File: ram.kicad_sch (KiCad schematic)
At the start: 8 parts, among them J1 ramslot1, J2 ramslot2, J3 ramslot3, J4 ramslot4, U24 74HC08, U29 74HC32, U30 74HC139

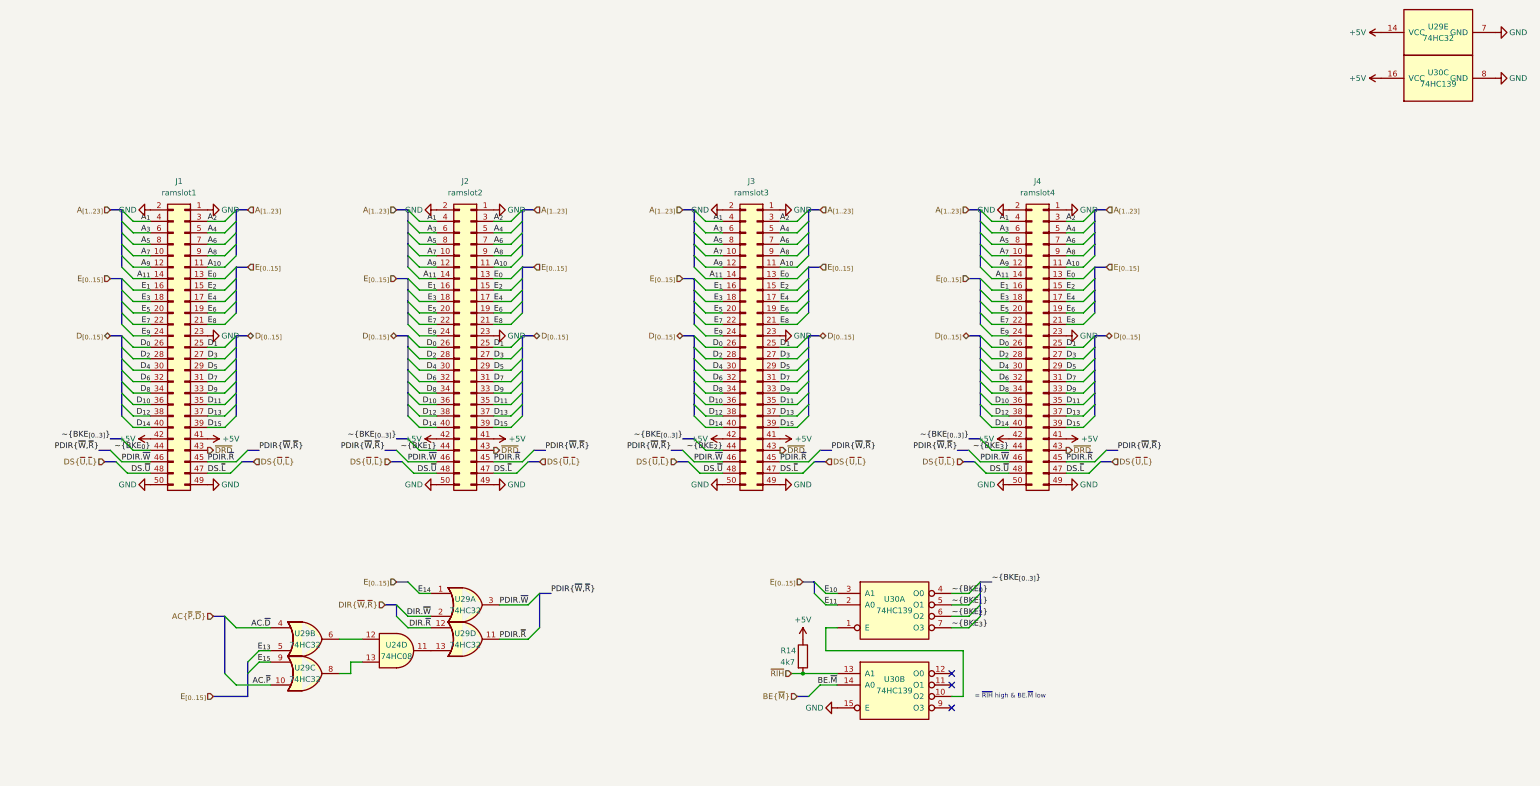
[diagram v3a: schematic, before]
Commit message: first commit: scheme ok [decoder]: 	- new spv. address space [mmu]: 	- removed pidreg 	- switched back to 8Kb mmu rams [ram/peripherals]: 	- added ground pins to connectors [misc]: 	- added DMA support 	- added clock halfer
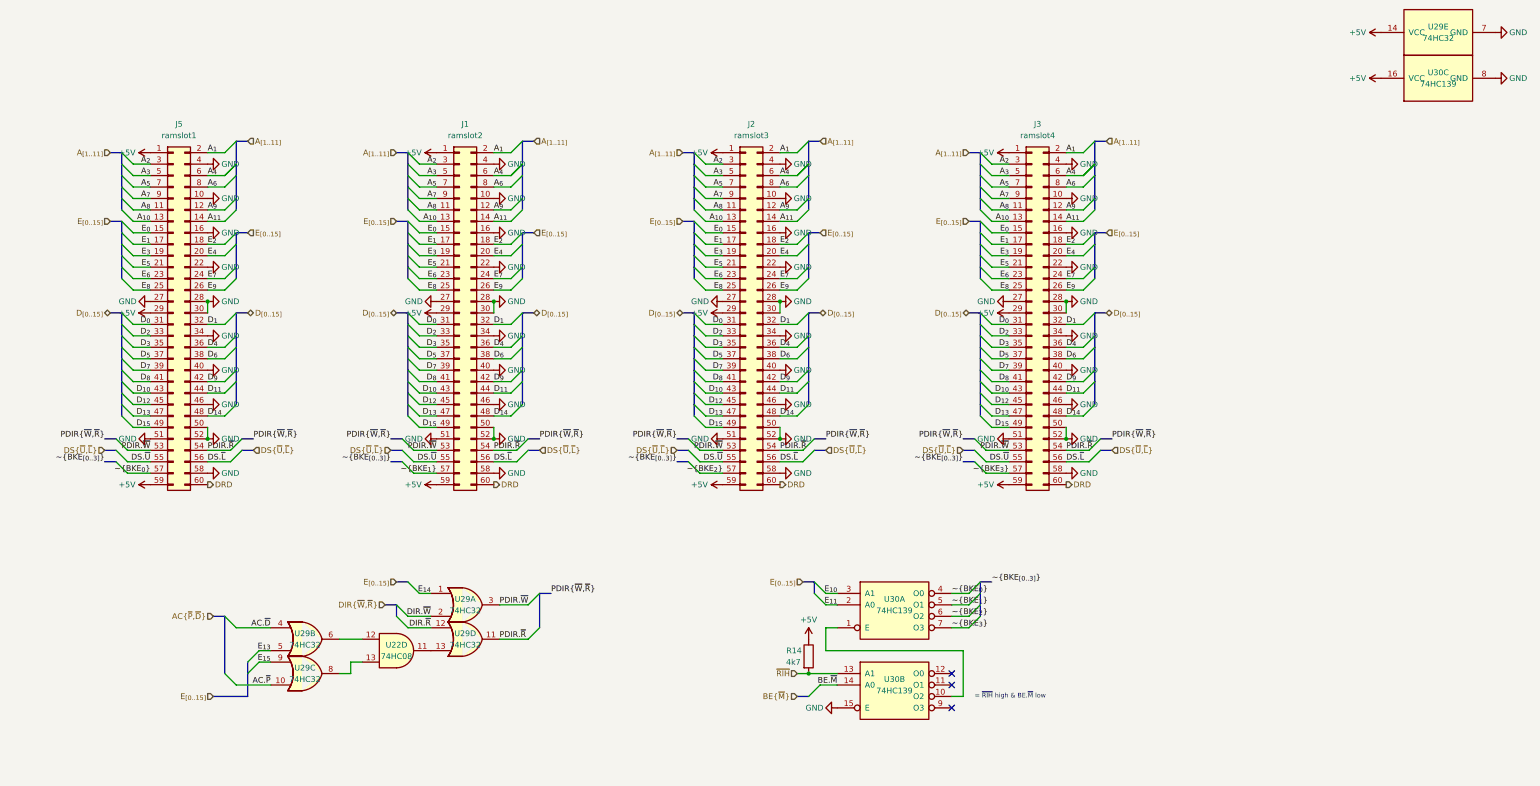
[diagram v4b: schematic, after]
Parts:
- removed J1: ramslot1, Connector_PCBEdge:TE_1-5530843-6, symbol Connector_Generic:Conn_02x25_Odd_Even
- removed J2: ramslot2, Connector_PCBEdge:TE_1-5530843-6, symbol Connector_Generic:Conn_02x25_Odd_Even
- removed J3: ramslot3, Connector_PCBEdge:TE_1-5530843-6, symbol Connector_Generic:Conn_02x25_Odd_Even
- removed J4: ramslot4, Connector_PCBEdge:TE_1-5530843-6, symbol Connector_Generic:Conn_02x25_Odd_Even
- removed U24: 74HC08, Package_DIP:DIP-14_W7.62mm, symbol 74xx:74LS08
- added J1: ramslot2, symbol Connector_Generic:Conn_02x30_Odd_Even
- added J2: ramslot3, symbol Connector_Generic:Conn_02x30_Odd_Even
- added J3: ramslot4, symbol Connector_Generic:Conn_02x30_Odd_Even
- added J5: ramslot1, symbol Connector_Generic:Conn_02x30_Odd_Even
- added U22: 74HC08, symbol 74xx:74LS08
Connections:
- net +5V: now also J1.1 (Pin_1), J1.29 (Pin_29), J1.59 (Pin_59), J2.1 (Pin_1), J2.29 (Pin_29), J2.59 (Pin_59), J3.1 (Pin_1), J3.29 (Pin_29), J3.59 (Pin_59), J5.1 (Pin_1), J5.29 (Pin_29), J5.59 (Pin_59)
- net A_{10}: now also J1.13 (Pin_13), J2.13 (Pin_13), J3.13 (Pin_13), J5.13 (Pin_13)
- net A_{11}: now also J1.14 (Pin_14), J2.14 (Pin_14), J3.14 (Pin_14), J5.14 (Pin_14)
- net A_{1}: now also J1.2 (Pin_2), J2.2 (Pin_2), J3.2 (Pin_2), J5.2 (Pin_2)
- net A_{2}: now also J1.3 (Pin_3), J2.3 (Pin_3), J3.3 (Pin_3), J5.3 (Pin_3)
- net A_{3}: now also J1.5 (Pin_5), J2.5 (Pin_5), J3.5 (Pin_5), J5.5 (Pin_5)
- net A_{4}: now also J1.6 (Pin_6), J2.6 (Pin_6), J3.6 (Pin_6), J5.6 (Pin_6)
- net A_{5}: now also J1.7 (Pin_7), J2.7 (Pin_7), J3.7 (Pin_7), J5.7 (Pin_7)
- net A_{6}: now also J1.8 (Pin_8), J2.8 (Pin_8), J3.8 (Pin_8), J5.8 (Pin_8)
- net A_{7}: now also J1.9 (Pin_9), J2.9 (Pin_9), J3.9 (Pin_9), J5.9 (Pin_9)
- net A_{8}: now also J1.11 (Pin_11), J2.11 (Pin_11), J3.11 (Pin_11), J5.11 (Pin_11)
- net A_{9}: now also J1.12 (Pin_12), J2.12 (Pin_12), J3.12 (Pin_12), J5.12 (Pin_12)
- net DS.~{L}: now also J1.56 (Pin_56), J2.56 (Pin_56), J3.56 (Pin_56), J5.56 (Pin_56)
- net DS.~{U}: now also J1.55 (Pin_55), J2.55 (Pin_55), J3.55 (Pin_55), J5.55 (Pin_55)
- net D_{0}: now also J1.31 (Pin_31), J2.31 (Pin_31), J3.31 (Pin_31), J5.31 (Pin_31)
- net D_{10}: now also J1.43 (Pin_43), J2.43 (Pin_43), J3.43 (Pin_43), J5.43 (Pin_43)
- net D_{11}: now also J1.44 (Pin_44), J2.44 (Pin_44), J3.44 (Pin_44), J5.44 (Pin_44)
- net D_{12}: now also J1.45 (Pin_45), J2.45 (Pin_45), J3.45 (Pin_45), J5.45 (Pin_45)
- net D_{13}: now also J1.47 (Pin_47), J2.47 (Pin_47), J3.47 (Pin_47), J5.47 (Pin_47)
- net D_{14}: now also J1.48 (Pin_48), J2.48 (Pin_48), J3.48 (Pin_48), J5.48 (Pin_48)
- net D_{15}: now also J1.49 (Pin_49), J2.49 (Pin_49), J3.49 (Pin_49), J5.49 (Pin_49)
- net D_{1}: now also J1.32 (Pin_32), J2.32 (Pin_32), J3.32 (Pin_32), J5.32 (Pin_32)
- net D_{2}: now also J1.33 (Pin_33), J2.33 (Pin_33), J3.33 (Pin_33), J5.33 (Pin_33)
- net D_{3}: now also J1.35 (Pin_35), J2.35 (Pin_35), J3.35 (Pin_35), J5.35 (Pin_35)
- net D_{4}: now also J1.36 (Pin_36), J2.36 (Pin_36), J3.36 (Pin_36), J5.36 (Pin_36)
- net D_{5}: now also J1.37 (Pin_37), J2.37 (Pin_37), J3.37 (Pin_37), J5.37 (Pin_37)
- net D_{6}: now also J1.38 (Pin_38), J2.38 (Pin_38), J3.38 (Pin_38), J5.38 (Pin_38)
- net D_{7}: now also J1.39 (Pin_39), J2.39 (Pin_39), J3.39 (Pin_39), J5.39 (Pin_39)
- net D_{8}: now also J1.41 (Pin_41), J2.41 (Pin_41), J3.41 (Pin_41), J5.41 (Pin_41)
- net D_{9}: now also J1.42 (Pin_42), J2.42 (Pin_42), J3.42 (Pin_42), J5.42 (Pin_42)
- net E_{0}: now also J1.15 (Pin_15), J2.15 (Pin_15), J3.15 (Pin_15), J5.15 (Pin_15)
- net E_{1}: now also J1.17 (Pin_17), J2.17 (Pin_17), J3.17 (Pin_17), J5.17 (Pin_17)
- net E_{2}: now also J1.18 (Pin_18), J2.18 (Pin_18), J3.18 (Pin_18), J5.18 (Pin_18)
- net E_{3}: now also J1.19 (Pin_19), J2.19 (Pin_19), J3.19 (Pin_19), J5.19 (Pin_19)
- net E_{4}: now also J1.20 (Pin_20), J2.20 (Pin_20), J3.20 (Pin_20), J5.20 (Pin_20)
- net E_{5}: now also J1.21 (Pin_21), J2.21 (Pin_21), J3.21 (Pin_21), J5.21 (Pin_21)
- net E_{6}: now also J1.23 (Pin_23), J2.23 (Pin_23), J3.23 (Pin_23), J5.23 (Pin_23)
- net E_{7}: now also J1.24 (Pin_24), J2.24 (Pin_24), J3.24 (Pin_24), J5.24 (Pin_24)
- net E_{8}: now also J1.25 (Pin_25), J2.25 (Pin_25), J3.25 (Pin_25), J5.25 (Pin_25)
- net E_{9}: now also J1.26 (Pin_26), J2.26 (Pin_26), J3.26 (Pin_26), J5.26 (Pin_26)
- net GND: now also J1.10 (Pin_10), J1.16 (Pin_16), J1.22 (Pin_22), J1.27 (Pin_27), J1.28 (Pin_28), J1.30 (Pin_30), J1.34 (Pin_34), J1.4 (Pin_4), J1.40 (Pin_40), J1.46 (Pin_46), J1.50 (Pin_50), J1.51 (Pin_51), J1.52 (Pin_52), J1.58 (Pin_58), J2.10 (Pin_10), J2.16 (Pin_16), J2.22 (Pin_22), J2.27 (Pin_27), J2.28 (Pin_28), J2.30 (Pin_30), J2.34 (Pin_34), J2.4 (Pin_4), J2.40 (Pin_40), J2.46 (Pin_46), J2.50 (Pin_50), J2.51 (Pin_51), J2.52 (Pin_52), J2.58 (Pin_58), J3.10 (Pin_10), J3.16 (Pin_16), J3.22 (Pin_22), J3.27 (Pin_27), J3.28 (Pin_28), J3.30 (Pin_30), J3.34 (Pin_34), J3.4 (Pin_4), J3.40 (Pin_40), J3.46 (Pin_46), J3.50 (Pin_50), J3.51 (Pin_51), J3.52 (Pin_52), J3.58 (Pin_58), J5.10 (Pin_10), J5.16 (Pin_16), J5.22 (Pin_22), J5.27 (Pin_27), J5.28 (Pin_28), J5.30 (Pin_30), J5.34 (Pin_34), J5.4 (Pin_4), J5.40 (Pin_40), J5.46 (Pin_46), J5.50 (Pin_50), J5.51 (Pin_51), J5.52 (Pin_52), J5.58 (Pin_58)
- net PDIR.~{R}: now also J1.54 (Pin_54), J2.54 (Pin_54), J3.54 (Pin_54), J5.54 (Pin_54)
- net PDIR.~{W}: now also J1.53 (Pin_53), J2.53 (Pin_53), J3.53 (Pin_53), J5.53 (Pin_53)
- net ~{BKE_{0}}: now also J5.57 (Pin_57)
- net ~{BKE_{1}}: now also J1.57 (Pin_57)
- net ~{BKE_{2}}: now also J2.57 (Pin_57)
- net ~{BKE_{3}}: now also J3.57 (Pin_57)
- net at U29.6: now also U22.12
- net at U29.13: now also U22.11
- net at U29.8: now also U22.13
- new net DRD: J1.60 (Pin_60), J2.60 (Pin_60), J3.60 (Pin_60), J5.60 (Pin_60)
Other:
- moved on the sheet: R14

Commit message: assigned footprints
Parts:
- J1, J2, J3, J5: footprint (none) -> Connector_TE-Connectivity:55308437
- U22: footprint (none) -> Package_DIP:DIP-14_W7.62mm
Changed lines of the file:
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@@
 			)
 		)
-		(property "Footprint" ""
+		(property "Footprint" "Connector_TE-Connectivity:55308437"
 			(at 240.03 62.23 0)
 			(effects
@@
 			)
 		)
-		(property "Footprint" ""
+		(property "Footprint" "Connector_TE-Connectivity:55308437"
 			(at 49.53 62.23 0)
 			(effects
@@
 			)
 		)
-		(property "Footprint" ""
+		(property "Footprint" "Connector_TE-Connectivity:55308437"
 			(at 176.53 62.23 0)
 			(effects
@@
 			)
 		)
-		(property "Footprint" ""
+		(property "Footprint" "Package_DIP:DIP-14_W7.62mm"
 			(at 99.06 137.16 0)
 			(effects
@@
 			)
 		)
-		(property "Footprint" ""
+		(property "Footprint" "Connector_TE-Connectivity:55308437"
 			(at 113.03 62.23 0)
 			(effects

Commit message: 1.0.0 commit
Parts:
- renumbered J1 to J6, J2 to J7, J3 to J9, R14 to R2, U30 to U16, U29 to U21, U22 to U25
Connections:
- net at U21.6: now also U25.9; no longer U25.12
- net at U21.13: now also U25.8; no longer U25.11
- net at U21.8: now also U25.10; no longer U25.13
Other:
- moved on the sheet: J5, J6, J7, J9, R2, U16A, U16B, U21A, U21B, U21C, U21D, U25C
